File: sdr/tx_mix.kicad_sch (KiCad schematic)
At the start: 7 parts, among them U12 74LVC1G66, U13 74LVC1G66, U14 74LVC1G66

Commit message: Complete layout
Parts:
- added C11: 10n, Capacitor_SMD:C_0402_1005Metric, symbol Device:C
- R33, R34: footprint (none) -> Resistor_SMD:R_0402_1005Metric
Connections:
- net +3.3V: now also C11.1
- net GND: now also C11.2
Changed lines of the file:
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@@
       (effects (font (size 1.27 1.27)) (justify left))
     )
-    (property "Footprint" "" (at 129.032 80.01 90)
+    (property "Footprint" "Resistor_SMD:R_0402_1005Metric" (at 129.032 80.01 90)
       (effects (font (size 1.27 1.27)) hide)
     )
@@
     )
   )
+  (symbol (lib_id "Device:C") (at 185.42 105.41 0) (unit 1)
+    (in_bom yes) (on_board yes) (dnp no) (fields_autoplaced)
+    (property "Reference" "C11" (at 189.23 104.1399 0)
+      (effects (font (size 1.27 1.27)) (justify left))
+    )
+    (property "Value" "10n" (at 189.23 106.6799 0)
+      (effects (font (size 1.27 1.27)) (justify left))
+    )
+    (property "Footprint" "Capacitor_SMD:C_0402_1005Metric" (at 186.3852 109.22 0)
+      (effects (font (size 1.27 1.27)) hide)
+    )
+    (property "Datasheet" "~" (at 185.42 105.41 0)
+      (effects (font (size 1.27 1.27)) hide)
+    )
+    (pin "1")
+    (pin "2")
+    (instances
+      (project "sdr"
+        (path "/ee974380-b45b-4b16-8475-50e4e51dc6cf/ad7b2242-3b39-40b3-b2e9-d6ea800dea9e"
+          (reference "C11") (unit 1)
+        )
+        (path "/ee974380-b45b-4b16-8475-50e4e51dc6cf/cebbb4d4-df0b-4a29-b2b2-0c76d3bf10e4"
+          (reference "C28") (unit 1)
+        )
+        (path "/ee974380-b45b-4b16-8475-50e4e51dc6cf/ae3469ea-e61f-4c82-bce0-cc247848c762"
+          (reference "C29") (unit 1)
+        )
+        (path "/ee974380-b45b-4b16-8475-50e4e51dc6cf/d0348644-e03f-4f7e-9ac7-cca0c2557a05"
+          (reference "C30") (unit 1)
+        )
+      )
+    )
+  )
+  (symbol (lib_id "power:+3.3V") (at 185.42 101.6 0) (unit 1)
+    (in_bom yes) (on_board yes) (dnp no) (fields_autoplaced)
+    (property "Reference" "#PWR050" (at 185.42 105.41 0)
+      (effects (font (size 1.27 1.27)) hide)
+    )
+    (property "Value" "+3.3V" (at 185.42 96.52 0)
+      (effects (font (size 1.27 1.27)))
+    )
+    (property "Footprint" "" (at 185.42 101.6 0)
+      (effects (font (size 1.27 1.27)) hide)
+    )
+    (property "Datasheet" "" (at 185.42 101.6 0)
+      (effects (font (size 1.27 1.27)) hide)
+    )
+    (pin "1")
+    (instances
+      (project "sdr"
+        (path "/ee974380-b45b-4b16-8475-50e4e51dc6cf/d0348644-e03f-4f7e-9ac7-cca0c2557a05"
+          (reference "#PWR050") (unit 1)
+        )
+      )
+    )
+  )
+  (symbol (lib_id "power:GND") (at 185.42 109.22 0) (unit 1)
+    (in_bom yes) (on_board yes) (dnp no) (fields_autoplaced)
+    (property "Reference" "#PWR054" (at 185.42 115.57 0)
+      (effects (font (size 1.27 1.27)) hide)
+    )
+    (property "Value" "GND" (at 185.42 114.3 0)
+      (effects (font (size 1.27 1.27)))
+    )
+    (property "Footprint" "" (at 185.42 109.22 0)
+      (effects (font (size 1.27 1.27)) hide)
+    )
+    (property "Datasheet" "" (at 185.42 109.22 0)
+      (effects (font (size 1.27 1.27)) hide)
+    )
+    (pin "1")
+    (instances
+      (project "sdr"
+        (path "/ee974380-b45b-4b16-8475-50e4e51dc6cf/d0348644-e03f-4f7e-9ac7-cca0c2557a05"
+          (reference "#PWR054") (unit 1)
+        )
+      )
+    )
+  )
   (symbol (lib_id "Device:C") (at 124.46 139.7 0) (unit 1)
     (in_bom yes) (on_board yes) (dnp no) (fields_autoplaced)
@@
       (effects (font (size 1.27 1.27)) (justify left))
     )
-    (property "Footprint" "" (at 129.032 101.6 90)
-      (effects (font (size 1.27 1.27)) hide)
-    )
+    (property "Footprint" "Resistor_SMD:R_0402_1005Metric" (at 129.032 101.6 90)
+      (effects (font (size 1.27 1.27)) hide)
+    )

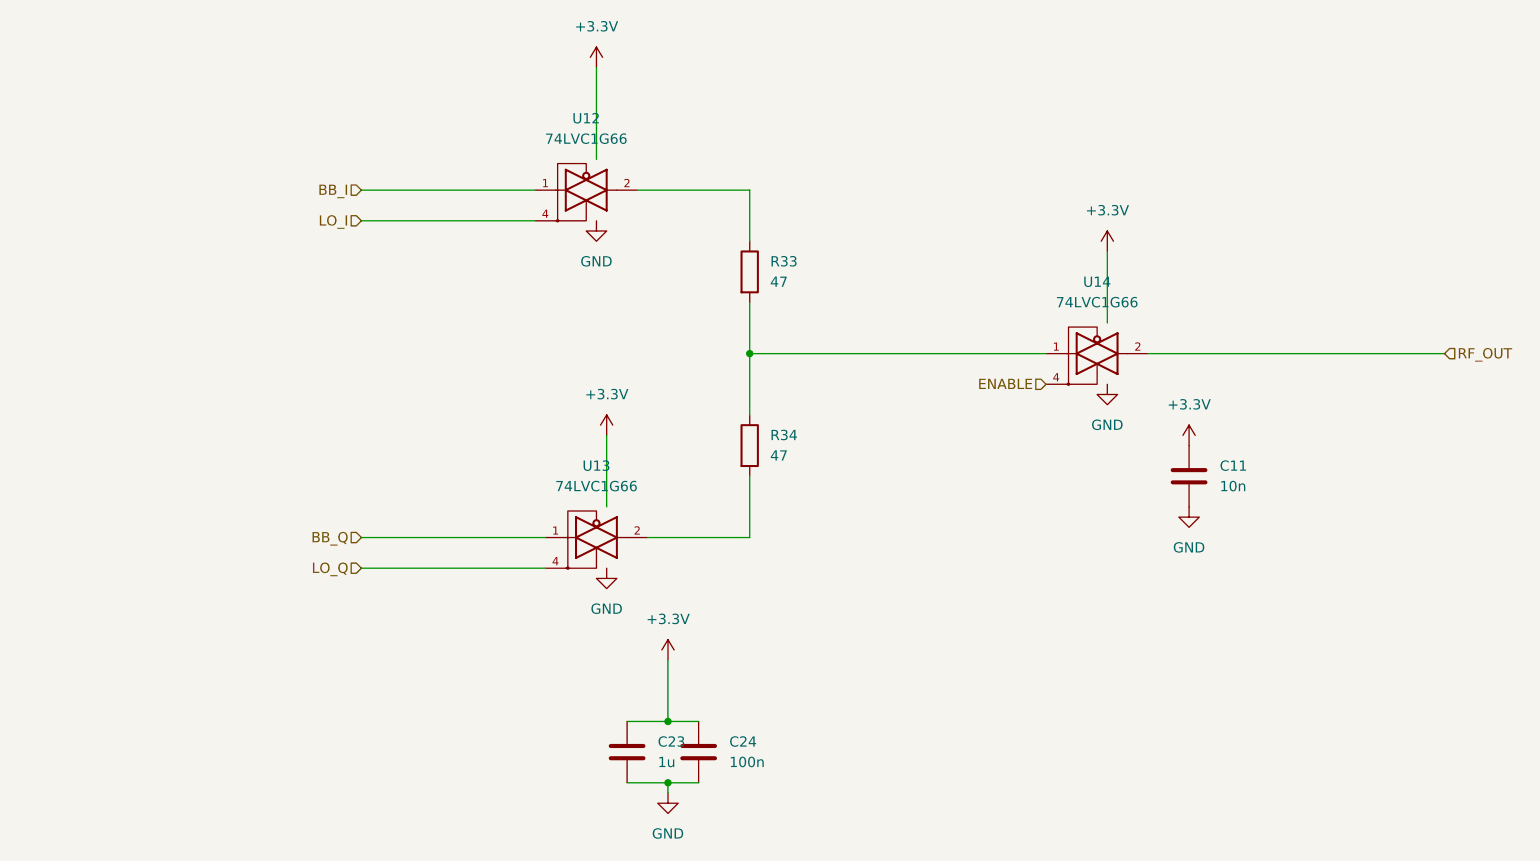
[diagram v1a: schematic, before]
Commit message: Update the via size. Reduce footprints outside board.
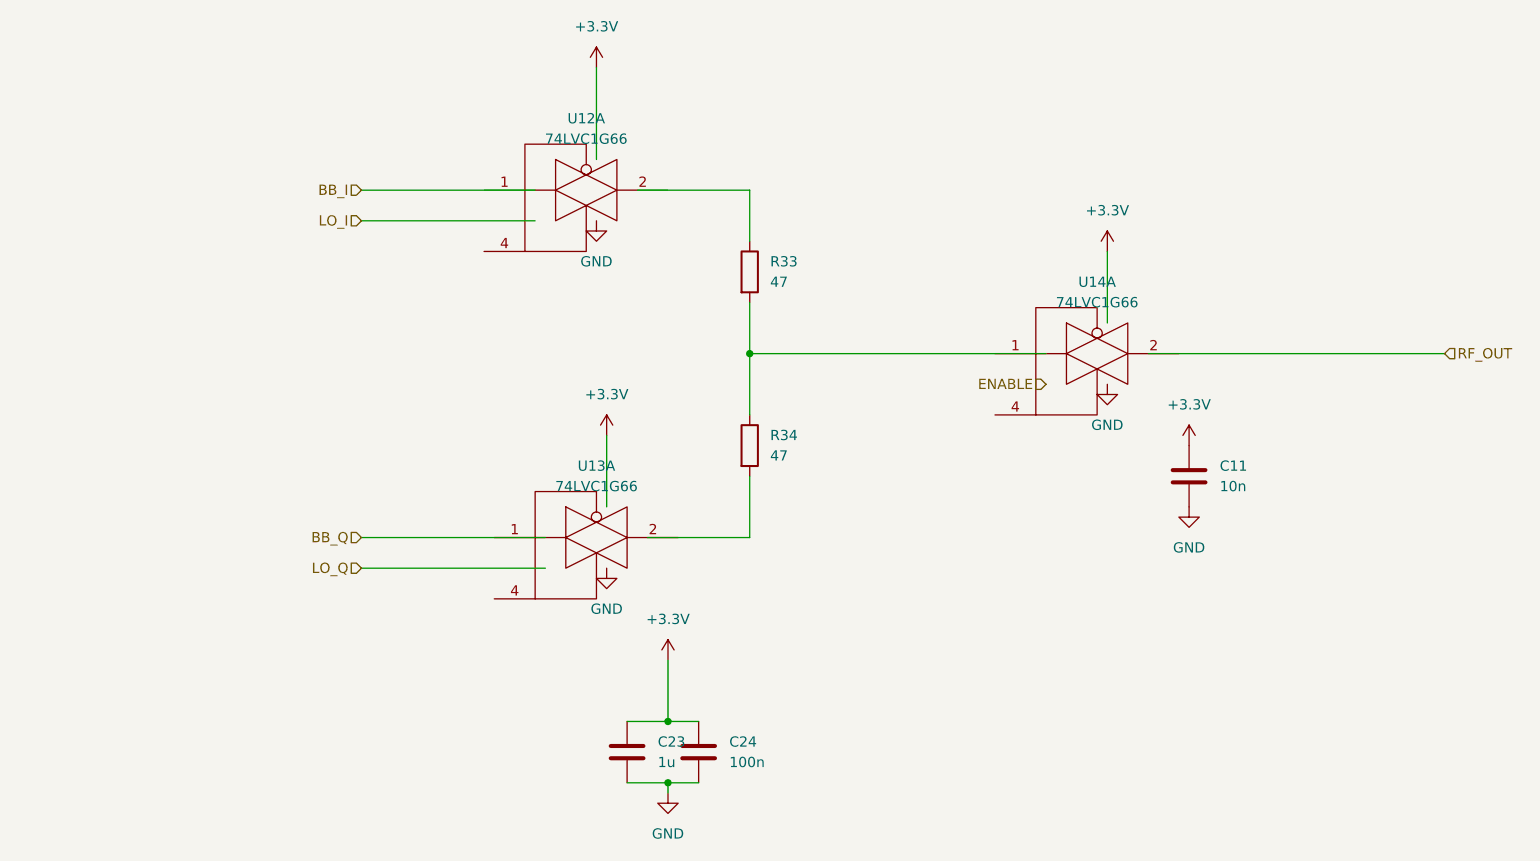
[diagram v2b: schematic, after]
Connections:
- net +3.3V: no longer U12.5 (VCC), U13.5 (VCC), U14.5 (VCC)
- net BB_I: no longer U12.1
- net BB_Q: no longer U13.1
- net ENABLE: no longer U14.4
- net GND: no longer U12.3 (GND), U13.3 (GND), U14.3 (GND)
- net LO_I: no longer U12.4
- net LO_Q: no longer U13.4
- net RF_OUT: no longer U14.2
- net at U12.2: no longer R33.1
- net at U13.2: no longer R34.2
- net at R33.2, R34.1: no longer U14.1
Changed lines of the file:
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@@
     (pin "1")
     (pin "2")
+    (pin "4")
     (pin "3")
+    (pin "5")
+    (instances
+      (project "sdr"
+        (path "/ee974380-b45b-4b16-8475-50e4e51dc6cf/d0348644-e03f-4f7e-9ac7-cca0c2557a05"
+          (reference "U12") (unit 1)
+        )
+      )
+    )
+  )
+  (symbol (lib_id "74xGxx:74LVC1G66") (at 111.76 113.03 0) (unit 1)
+    (in_bom yes) (on_board yes) (dnp no) (fields_autoplaced)
+    (property "Reference" "U13" (at 111.76 104.14 0)
+      (effects (font (size 1.27 1.27)))
+    )
+    (property "Value" "74LVC1G66" (at 111.76 106.68 0)
+      (effects (font (size 1.27 1.27)))
+    )
+    (property "Footprint" "Package_TO_SOT_SMD:SOT-353_SC-70-5" (at 111.76 113.03 0)
+      (effects (font (size 1.27 1.27)) hide)
+    )
+    (property "Datasheet" "http://www.ti.com/lit/ds/symlink/sn74lvc1g66.pdf" (at 111.76 113.03 0)
+      (effects (font (size 1.27 1.27)) hide)
+    )
+    (pin "1")
+    (pin "2")
     (pin "4")
-    (pin "5")
-    (instances
-      (project "sdr"
-        (path "/ee974380-b45b-4b16-8475-50e4e51dc6cf/d0348644-e03f-4f7e-9ac7-cca0c2557a05"
-          (reference "U12") (unit 1)
-        )
-      )
-    )
-  )
-  (symbol (lib_id "74xGxx:74LVC1G66") (at 111.76 113.03 0) (unit 1)
-    (in_bom yes) (on_board yes) (dnp no) (fields_autoplaced)
-    (property "Reference" "U13" (at 111.76 104.14 0)
-      (effects (font (size 1.27 1.27)))
-    )
-    (property "Value" "74LVC1G66" (at 111.76 106.68 0)
-      (effects (font (size 1.27 1.27)))
-    )
-    (property "Footprint" "Package_TO_SOT_SMD:SOT-353_SC-70-5" (at 111.76 113.03 0)
-      (effects (font (size 1.27 1.27)) hide)
-    )
-    (property "Datasheet" "http://www.ti.com/lit/ds/symlink/sn74lvc1g66.pdf" (at 111.76 113.03 0)
-      (effects (font (size 1.27 1.27)) hide)
-    )
-    (pin "1")
-    (pin "2")
     (pin "3")
-    (pin "4")
     (pin "5")
     (instances
@@
     (pin "1")
     (pin "2")
+    (pin "4")
     (pin "3")
-    (pin "4")
     (pin "5")
     (instances

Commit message: Convert to a 4-layer board.
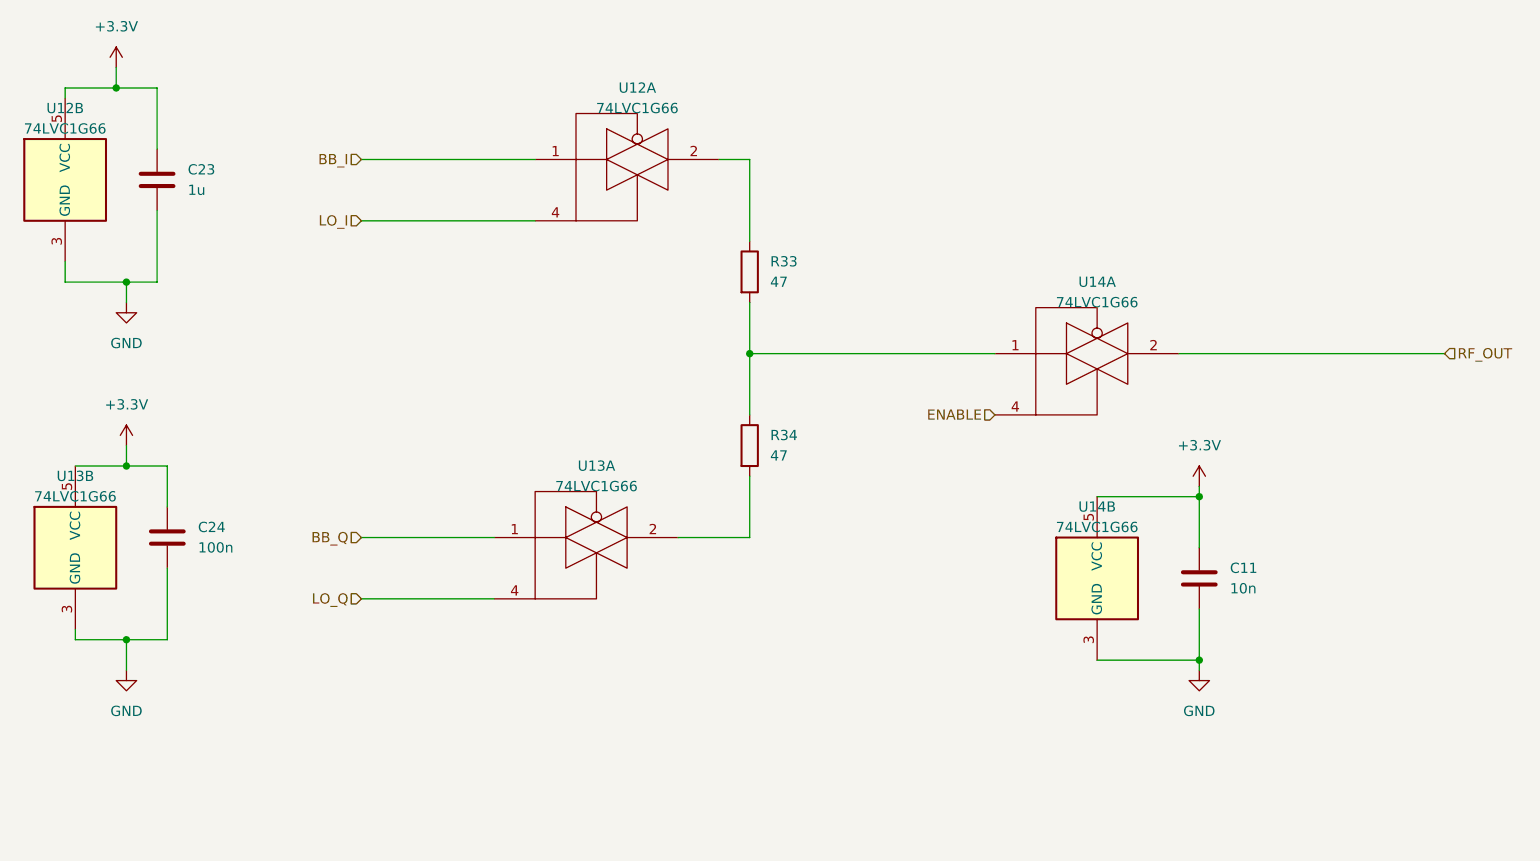
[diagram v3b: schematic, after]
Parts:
- added unit 2 of U12
- added unit 2 of U13
- added unit 2 of U14
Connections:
- net +3.3V: now also U12.5 (VCC), U13.5 (VCC), U14.5 (VCC)
- net BB_I: now also U12.1
- net BB_Q: now also U13.1
- net ENABLE: now also U14.4
- net GND: now also U12.3 (GND), U13.3 (GND), U14.3 (GND)
- net LO_I: now also U12.4
- net LO_Q: now also U13.4
- net RF_OUT: now also U14.2
- net at U12.2: now also R33.1
- net at U13.2: now also R34.2
- net at R33.2, R34.1: now also U14.1
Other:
- moved on the sheet: C11, C23, C24, U12A
